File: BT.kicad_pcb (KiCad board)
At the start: 4 copper layers, 55 x 40 mm, 84 parts, among them J1 Conn_01x05_Pin, J2 Conn_01x03_Pin, J3 Conn_01x06_Pin, J5 Conn_02x03_Odd_Even, K1 AGQ200S12Z, Q1 BSS123, U1 PCM5100A, U2 ESP32-WROOM-32U, U3 TLV4888DR, U4 AP64060WU-7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

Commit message: integrated DAC in database
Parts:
- U1: footprint Package_SO:TSSOP-20_4.4x6.5mm_P0.65mm -> NRD_IC_DATA:PCM510xx
- moved C11 178.1 mm to (311.1, 121.3), turned to 0 degrees
- moved C7 176.0 mm to (311.1, 118.8), turned to 0 degrees
- moved C13 175.6 mm to (315.3, 119.0), turned to 0 degrees
- moved C12 174.1 mm to (311.1, 123.8), turned to 0 degrees
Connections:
- net Net-(U4-EN) renamed /+12V_FUSED

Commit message: wip
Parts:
- removed C28: 100nF, NRD_CAP:C_0603
- removed J5: Conn_02x03_Odd_Even, Connector_PinHeader_1.27mm:PinHeader_2x03_P1.27mm_Vertical_SMD
- removed L1, L2: 8.2uH, NRD_IND:74438367082
- removed U7: AP64060WU-7, NRD_IC_DCDC:AP6406x
- added C22: 2.2uF, NRD_CAP:C_0805, F.Cu at (182.1, 89.5)
- added C23: 4.7uF, NRD_CAP:C_1206, F.Cu at (196.0, 89.7)
- added C33: 2.2uF, NRD_CAP:C_0805, F.Cu at (182.1, 92.5)
- added C34: 2.2uF, NRD_CAP:C_0805, F.Cu at (182.1, 95.5)
- added C35: 100nF, NRD_CAP:C_0603, F.Cu at (181.9, 101.3)
- added C36: 2.2uF, NRD_CAP:C_0805, F.Cu at (182.1, 98.5)
- added FB2: 4k7@100MHz, Inductor_SMD:L_0805_2012Metric, F.Cu at (195.5, 92.7)
- added FB4: 4k7@100MHz, Inductor_SMD:L_0805_2012Metric, F.Cu at (195.5, 95.5)
- added J4: Boxed_Header_02x03_SMT, NRD_CON:Boxed_Header_02x03_SMT, F.Cu at (145.0, 102.2)
- added R32: 13K7, NRD_RES:R_0603, F.Cu at (181.9, 103.8)
- added RV1: 10K, Potentiometer_SMD:Potentiometer_Bourns_TC33X_Vertical, F.Cu at (152.8, 90.8)
- added U5: TLVM23615RDNR, NRD_IC_DCDC:TxxM336x5, F.Cu at (187.5, 103.1)
- C11, C7: footprint NRD_CAP:C_0603 -> NRD_CAP:C_0805
- C14, C15: value 220nF -> 2.2uF; footprint NRD_CAP:C_0603 -> NRD_CAP:C_0805
- C17: value 100nF -> 4.7uF; footprint NRD_CAP:C_0603 -> NRD_CAP:C_1206
- C18: value 2.2uF -> 100nF
- C19: value 10uF -> 4.7uF; footprint NRD_CAP:C_0805 -> NRD_CAP:C_1206
- C20: value 22uF -> 100nF; footprint NRD_CAP:C_0805 -> NRD_CAP:C_0603
- C21: value 22uF -> 4.7uF; footprint NRD_CAP:C_0805 -> NRD_CAP:C_1206
- C24, C25: value 10uF -> 22uF; footprint NRD_CAP:C_0805 -> NRD_CAP:C_1206
- C26: value 1uF -> 4.7uF; footprint NRD_CAP:C_0603 -> NRD_CAP:C_1206
- C29: value 2.2uF -> 22uF; footprint NRD_CAP:C_0603 -> NRD_CAP:C_1206
- C30: value 100nF -> 22uF; footprint NRD_CAP:C_0603 -> NRD_CAP:C_1206
- C31, C32: value 10uF -> 100nF; footprint NRD_CAP:C_0805 -> NRD_CAP:C_0603
- J3: value Conn_01x06_Pin -> S6B-PH-K-S; footprint Connector_JST:JST_PH_S6B-PH-K_1x06_P2.00mm_Horizontal -> NRD_CON:S6B-PH-K-S
- Q1: footprint Package_TO_SOT_SMD:SOT-23 -> NRD_MOSFET:BSS123
- R17, R19: value 0R -> 10K
- R18: value 2K -> 10K
- R2: value 10K -> 34K; footprint NRD_R_Var:3296P -> NRD_RES:R_0603
- R20: value 35K7 -> 2K
- R31: value 11K5 -> 21K
- R5: value 13K -> 14K3
- U2: footprint RF_Module:ESP32-WROOM-32U -> NRD_IC_MCU:WROOM_32U
- U4: value AP64060WU-7 -> TLVM23615RDNR; footprint NRD_IC_DCDC:AP6406x -> NRD_IC_DCDC:TxxM336x5
- U6: value TPS7A4701 -> RAA214220; footprint NRD_LDO:TPS7A47x -> NRD_LDO:RAA214220
- moved R2 37.7 mm to (186.4, 110.4)
- moved J3 5.55 mm to (171.6, 88.7)
- moved TP1 4.10 mm to (145.2, 92.0)
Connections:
- C17 pad 1: /BST_+6V -> +12V
- C17 pad 2: Net-(U4-SW) -> GND
- C18 pad 1: /+12V_FUSED -> +12V
- C19 pad 1: +5V -> +12V
- C20 pad 1: +3.3VA -> +12V
- C21 pad 1: +3.3VA -> Net-(U6-VOUT)
- C24 pad 1: +6V -> +3V3
- C25 pad 1: +6V -> +3V3
- C26 pad 1: Net-(U6-NR) -> Net-(U5-VCC)
- C27 pad 1: +5V -> Net-(U3E-V+)
- C30 pad 1: /BST_+3V3 -> +6V
- C30 pad 2: Net-(U7-SW) -> GND
- C32 pad 1: +3V3 -> Net-(C32-Pad1)
- F1 pad 1: /+12V_FUSED -> +12V
- F1 pad 2: +12V -> /KL30
- J3 pad 1: +12V -> /KL30
- R17 pad 1: Net-(U6-0.1V) -> +6V
- R17 pad 2: GND -> Net-(U5-FB)
- R18 pad 1: /FB_+6V -> Net-(U4-RT)
- R19 pad 1: Net-(U6-3.2V) -> Net-(U5-RT)
- R2 pad 1: Net-(C14-Pad2) -> +3V3
- R2 pad 2: GND -> Net-(U4-FB)
- R20 pad 1: +3V3 -> Net-(U5-FB)
- R20 pad 2: /FB_+3V3 -> GND
- R25 pad 1: Net-(R2-Pad3) -> Net-(R25-Pad1)
- R26 pad 2: Net-(R2-Pad3) -> Net-(R25-Pad1)
- R29 pad 2: Net-(R2-Pad3) -> Net-(R25-Pad1)
- R31 pad 1: /FB_+3V3 -> Net-(U6-VOUT)
- R31 pad 2: GND -> Net-(U6-ADJ)
- R5 pad 1: +6V -> Net-(U4-FB)
- R5 pad 2: /FB_+6V -> GND
- U3 pad 4: +5V -> Net-(U3E-V+)
- U4 pad 1: /BST_+6V -> unconnected-(U4-PGOOD-Pad1)
- U4 pad 2: GND -> +12V
- U4 pad 3: /FB_+6V -> +12V
- U4 pad 4: /+12V_FUSED -> +3V3
- U4 pad 5: /+12V_FUSED -> unconnected-(U4-SW-Pad5)_4
- U4 pad 6: Net-(U4-SW) -> unconnected-(U4-SW_2-Pad6)
- U6 pad 1: +3.3VA -> +3V3
- U6 pad 2: unconnected-(U6-NC-Pad2) -> GND
- U6 pad 3: +3.3VA -> +3V3
- U6 pad 4: unconnected-(U6-6.4V-Pad4) -> Net-(U6-ADJ)
- U6 pad 5: unconnected-(U6-6.4V-Pad5) -> Net-(U6-VOUT)

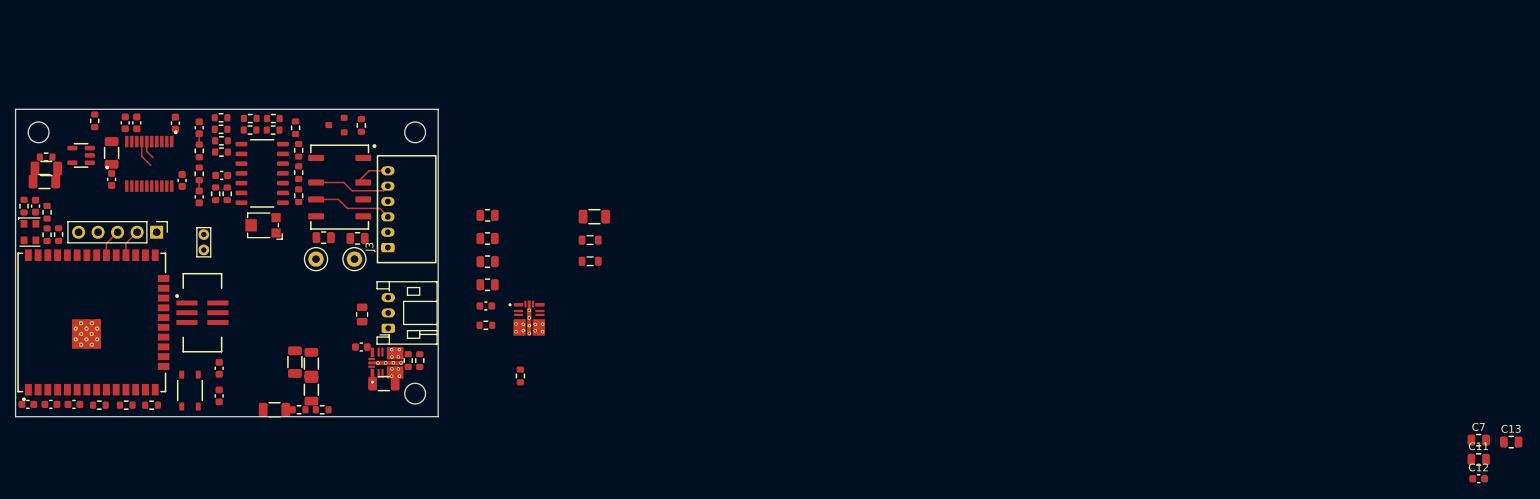
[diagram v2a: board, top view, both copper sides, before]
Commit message: rough placement PSU
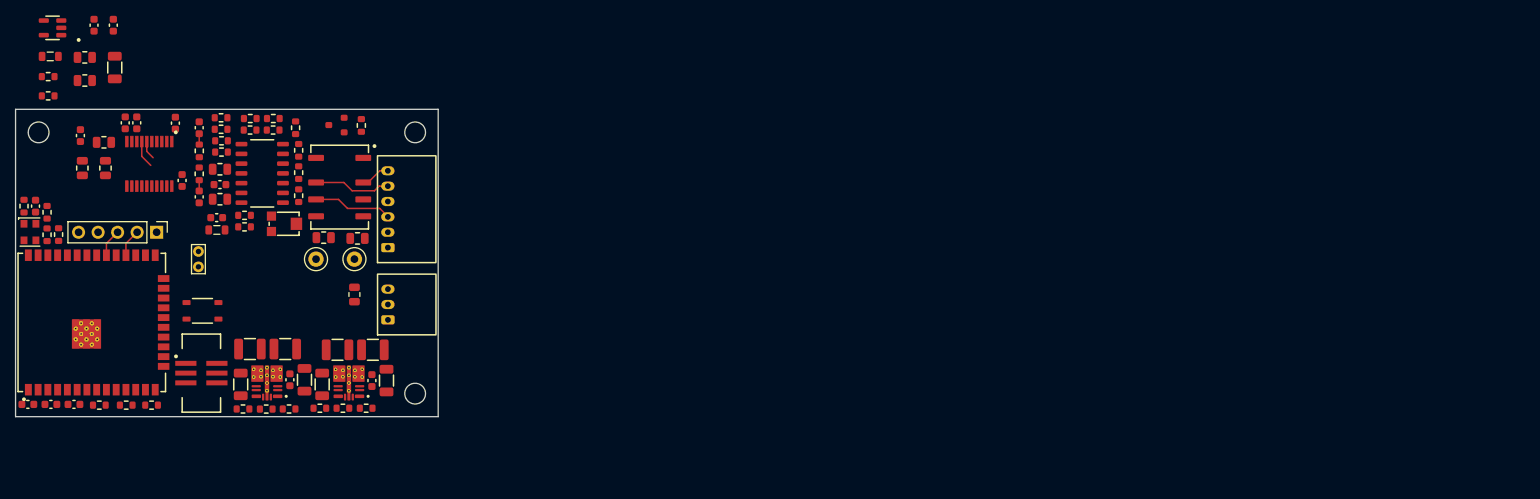
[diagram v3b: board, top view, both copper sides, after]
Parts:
- removed RV1: 10K, Potentiometer_SMD:Potentiometer_Bourns_TC33X_Vertical
- added R33: 10K, NRD_R_Var:TC33X-2, F.Cu at (155.8, 90.6)
- C24, C25, C29, C30: footprint NRD_CAP:C_1206 -> NRD_CAP:C_1210
- J2: value Conn_01x03_Pin -> S3B-PH-K-S; footprint Connector_JST:JST_PH_S3B-PH-K_1x03_P2.00mm_Horizontal -> NRD_CON:S3B-PH-K-S
- S1: value ~ -> 434123025826
- moved C12 187.4 mm to (129.1, 79.1), turned to 90 degrees
- moved C13 186.4 mm to (132.4, 83.4), turned to 90 degrees
- moved C11 185.6 mm to (129.4, 83.4), turned to 90 degrees
- moved C7 183.1 mm to (132.2, 80.0)
- moved FB2 74.2 mm to (125.2, 68.8)
- moved R32 64.3 mm to (124.9, 74.0)
- moved C22 56.3 mm to (129.7, 69.0)
- moved C33 56.3 mm to (129.7, 72.0)
- moved R31 56.1 mm to (124.9, 71.5)
- moved C31 50.9 mm to (130.9, 64.8)
- moved FB4 48.7 mm to (146.9, 91.4), turned to 180 degrees
- moved C32 46.7 mm to (133.4, 64.8)
- moved R19 45.2 mm to (156.3, 114.7), turned to 0 degrees
- moved C20 42.8 mm to (167.1, 111.0), turned to 90 degrees
- moved C19 42.6 mm to (158.3, 110.9), turned to 90 degrees
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
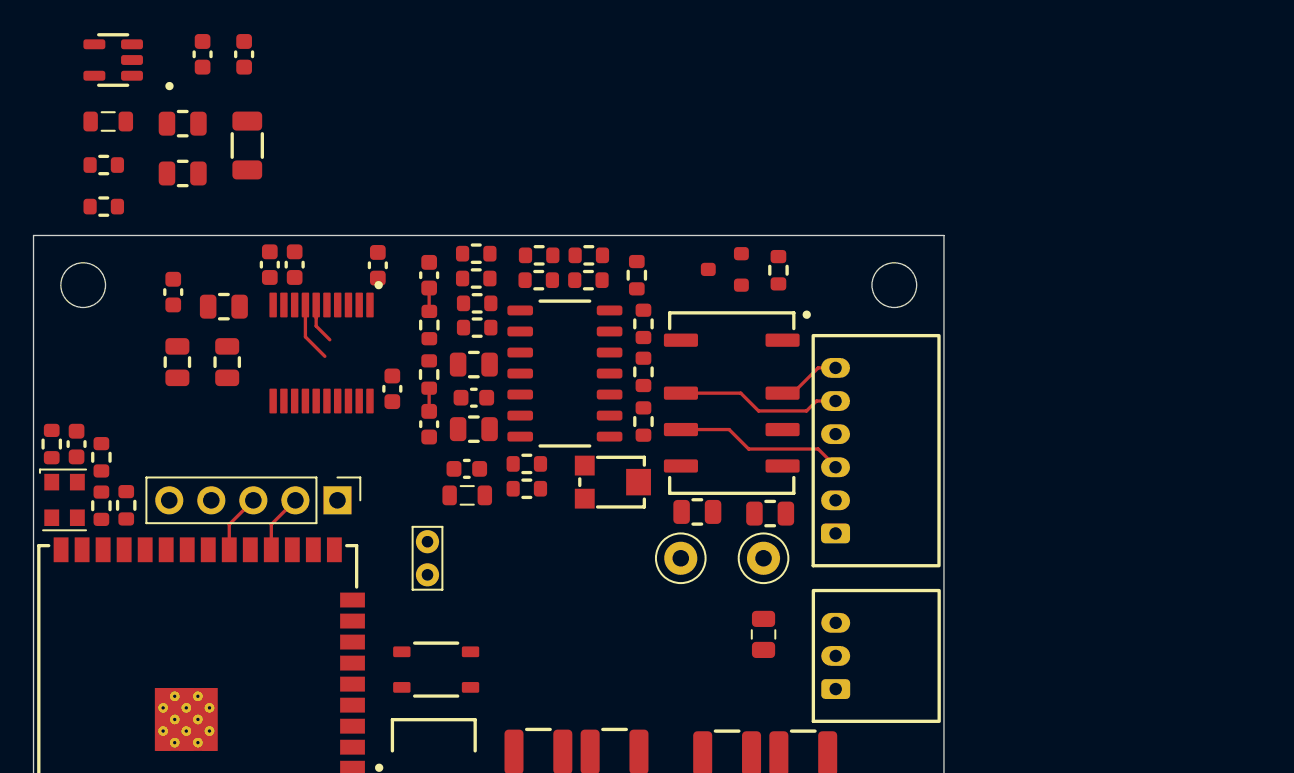
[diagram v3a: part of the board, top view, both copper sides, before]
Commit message: replaced all components by library parts
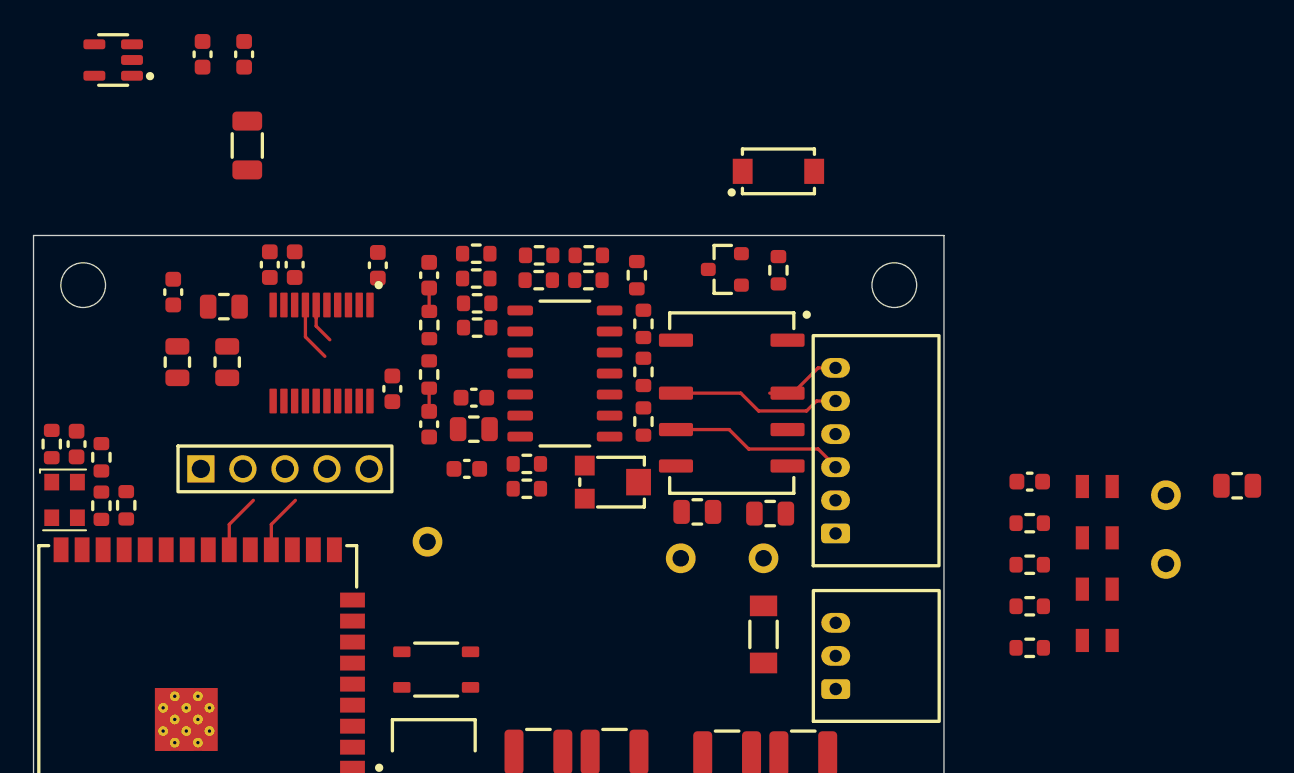
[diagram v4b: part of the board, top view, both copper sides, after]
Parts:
- removed C34: 2.2uF, NRD_CAP:C_0805
- removed FB2, FB4: 4k7@100MHz, Inductor_SMD:L_0805_2012Metric
- added D1: VSSAF5N50-M3/6B, NRD_Diodes:VSSAF5N50, F.Cu at (165.7, 71.8)
- added L1: 10uH, NRD_IND:74479777310, F.Cu at (184.9, 90.9)
- added L2: 10uH, NRD_IND:74479777310, F.Cu at (184.9, 94.0)
- added L3: 10uH, NRD_IND:74479777310, F.Cu at (184.9, 97.1)
- added L4: 10uH, NRD_IND:74479777310, F.Cu at (184.9, 100.2)
- added R34: 10K, NRD_RES:R_0603, F.Cu at (180.9, 98.1)
- added R35: 1K, NRD_RES:R_0603, F.Cu at (180.9, 100.6)
- added TP4: 5001, NRD_MISC:500x, F.Cu at (189.1, 91.4)
- added TP5: 5001, NRD_MISC:500x, F.Cu at (189.1, 95.5)
- C22: value 2.2uF -> 100nF; footprint NRD_CAP:C_0805 -> NRD_CAP:C_0603
- F1: value Fuse -> SF-1206S050-2; footprint Fuse:Fuse_0805_2012Metric -> NRD_Fuse:SF-1206S
- J1: value Conn_01x05_Pin -> 61300511121; footprint Connector_PinHeader_2.54mm:PinHeader_1x05_P2.54mm_Vertical -> NRD_PinHeader:61300511121
- J2: value S3B-PH-K-S -> Conn_01x03_Pin
- K1: value AGQ200S12Z -> AGQ200A12Z; footprint NRD_Relays:AGQ200Sxxx -> NRD_Relays:AGQ200Axxx
- M1: renamed from H1; value MountingHole -> (none); footprint MountingHole:MountingHole_2.7mm_M2.5_ISO7380 -> NRD_MECH:Mounting_Hole_2.7mm_Unplated
- M2: renamed from H2; value MountingHole -> (none); footprint MountingHole:MountingHole_2.7mm_M2.5_ISO7380 -> NRD_MECH:Mounting_Hole_2.7mm_Unplated
- M3: renamed from H3; value MountingHole -> (none); footprint MountingHole:MountingHole_2.7mm_M2.5_ISO7380 -> NRD_MECH:Mounting_Hole_2.7mm_Unplated
- S1: value 434123025826 -> Untitled
- TP1: value TestPoint -> 5001; footprint TestPoint:TestPoint_Bridge_Pitch2.0mm_Drill0.7mm -> NRD_MISC:500x
- TP2, TP3: value TestPoint -> 5001; footprint TestPoint:TestPoint_Loop_D2.50mm_Drill1.0mm -> NRD_MISC:500x
- moved C33 66.4 mm to (193.4, 90.8)
- moved R31 60.0 mm to (180.9, 93.1)
- moved R32 60.0 mm to (180.9, 95.6)
- moved C22 55.5 mm to (180.9, 90.6)
- moved J1 3.70 mm to (135.9, 89.8), turned to 0 degrees
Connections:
- net /DAC_MUTE renamed /DAC_MUTEn
- net Net-(U6-ADJ) renamed /+3V3A_FB
- C21 pad 1: Net-(U6-VOUT) -> /+3V3A_OUT
- C22 pad 1: Net-(U6-VOUT) -> /Button
- J2 pad 2: /Button -> Net-(J2-Pin_2)
- R31 pad 1: Net-(U6-VOUT) -> /+3V3A_OUT
- R7 pad 2: GND -> +3V3
- U6 pad 5: Net-(U6-VOUT) -> /+3V3A_OUT
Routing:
- net /DIN: track 3.59 -> 0.00 mm
- net /BCK: track 0.00 -> 3.59 mm

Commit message: started layout
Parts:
- removed TP4, TP5: 5001, NRD_MISC:500x
- J2: value Conn_01x03_Pin -> S3B-PH-K-S
- M1, M2, M3: value (none) -> Mounting_Hole_2.7mm_Unplated
- S1: value Untitled -> 434123025826
- moved C33 62.1 mm to (132.7, 77.7), turned to 90 degrees
- moved L3 59.0 mm to (128.6, 79.5), turned to 90 degrees
- moved L4 58.1 mm to (130.7, 79.5), turned to -90 degrees
- moved R31 52.6 mm to (129.1, 84.1)
- moved R34 50.5 mm to (139.5, 69.3)
- moved R32 50.2 mm to (132.0, 84.1)
- moved C22 49.1 mm to (137.3, 113.2)
- moved R35 48.3 mm to (134.3, 113.2)
- moved L2 38.1 mm to (147.3, 87.9)
- moved L1 37.7 mm to (147.3, 91.4), turned to 180 degrees
- moved R6 32.8 mm to (166.0, 103.1), turned to 180 degrees
- moved R17 20.9 mm to (169.4, 106.2), turned to 180 degrees
- moved C31 20.2 mm to (122.8, 83.2)
- moved C17 19.1 mm to (149.9, 109.3), turned to -90 degrees
- moved C11 19.0 mm to (144.0, 71.1)
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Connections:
- net Net-(J2-Pin_1) renamed /LED_CON
- net Net-(J2-Pin_2) renamed /BUTTON_CON
- net Net-(U4-FB) renamed /FB_+3V3
- J1 pad 2: /LRCK -> /BCK
- J1 pad 4: /BCK -> /LRCK
- U2 pad 28: /BCK -> /LRCK
- U2 pad 29: unconnected-(U2-IO5-Pad29) -> /DIN
- U2 pad 30: /LRCK -> unconnected-(U2-IO18-Pad30)
- U2 pad 31: /DIN -> /BCK
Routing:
- net Net-(C14-Pad2): track 0.00 -> 42.2 mm, vias 0 -> 2
- net +6V: track 0.00 -> 40.1 mm, vias 0 -> 3
- net GND: track 0.00 -> 38.0 mm, vias 0 -> 32
- net /ESP_EN: track 0.00 -> 36.2 mm, vias 0 -> 3
- net +12V: track 0.00 -> 34.5 mm, vias 0 -> 2
- net /ESP_RXD0: track 0.00 -> 30.2 mm
- net /ESP_TXD0: track 0.00 -> 26.7 mm
- net +3V3: track 0.00 -> 26.5 mm, vias 0 -> 8
- net /ESP_IO0: track 0.00 -> 21.5 mm
- net Net-(C8-Pad1): track 1.40 -> 21.0 mm, vias 0 -> 2
- net Net-(R25-Pad1): track 0.00 -> 18.6 mm, vias 0 -> 2
- net Net-(U3B-+): track 0.00 -> 15.9 mm, vias 0 -> 2
- net /KL30: track 0.00 -> 12.0 mm
- net /SCK: track 0.00 -> 11.8 mm, vias 0 -> 1
- net Net-(U3C-+): track 0.00 -> 10.1 mm
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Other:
- board text added: "+3V3"
- board text added: "BCK"
- board text added: "DIN"
- board text added: "GND"
- board text added: "LRCK"

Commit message: almost finished layout. Something is still off in the design rules
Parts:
- J2: value S3B-PH-K-S -> Conn_01x03_Pin
- M1, M2, M3: value Mounting_Hole_2.7mm_Unplated -> (none)
- S1: value 434123025826 -> Untitled
- moved R34 22.8 mm to (128.0, 88.9), turned to -90 degrees
- moved C12 21.9 mm to (138.8, 88.2), turned to 180 degrees
- moved C13 17.8 mm to (142.0, 88.2), turned to 0 degrees
- moved C7 12.5 mm to (140.1, 78.3), turned to 180 degrees
- moved C11 9.24 mm to (137.4, 77.6)
- moved TP1 8.36 mm to (152.8, 95.2)
- moved J1 2.47 mm to (135.9, 91.0)
- moved R15 1.20 mm to (125.0, 87.0)
- moved C8 0.85 mm to (144.9, 89.0)
- moved R6 0.83 mm to (166.2, 102.3), turned to 90 degrees
- moved C5 0.73 mm to (122.3, 113.9)
- moved C6 0.73 mm to (125.3, 113.9)
- moved C10 0.73 mm to (128.3, 113.9), turned to 180 degrees
- moved R3 0.73 mm to (131.3, 113.9)
- moved R35 0.73 mm to (134.3, 113.9)
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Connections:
- C3 pad 1: +3.3VA -> +3V3A
- C4 pad 1: +3.3VA -> +3V3A
- U1 pad 8: +3.3VA -> +3V3A
- U2 pad 10: /DAC_FMT -> unconnected-(U2-IO25-Pad10)
- U2 pad 30: unconnected-(U2-IO18-Pad30) -> /DAC_FLT
- U2 pad 33: /DAC_FLT -> /DAC_FMT
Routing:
- net /SW_TO_BT_AUDIO: track 0.00 -> 77.0 mm, vias 0 -> 2
- net /BUTTON_CON: track 1.01 -> 42.4 mm
- net /LED: track 0.00 -> 37.6 mm, vias 0 -> 2
- net GND: track 38.0 -> 73.0 mm, vias 32 -> 58
- net /DAC_MCLK_EN: track 0.00 -> 28.4 mm, vias 0 -> 2
- net /DAC_MUTEn: track 0.00 -> 26.3 mm, vias 0 -> 3
- net /DAC_DMP: track 0.00 -> 18.7 mm
- net /DAC_FMT: track 0.00 -> 16.5 mm
- net Net-(R24-Pad1): track 2.00 -> 17.6 mm, vias 0 -> 2
- net /DAC_FLT: track 0.00 -> 13.5 mm, vias 0 -> 2
- net /MCLK: track 0.00 -> 12.1 mm, vias 0 -> 2
- net +3V3: track 26.5 -> 33.7 mm, vias 8 -> 12
- net /SCK: track 11.8 -> 17.6 mm, vias 1 -> 2
- net /+3V3A_FB: track 0.00 -> 5.28 mm
- net Net-(U1-LDOO): track 0.00 -> 3.78 mm
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- added copper zone on F.Cu, net +12V
- added copper zone on F.Cu, net +3V3
- added copper zone on In2.Cu, net +3V3
- added copper zone on F.Cu, net +3V3A
- added copper zone on F.Cu, net /+3V3A_OUT
- added copper zone on B.Cu, net GND
- added copper zone on F.Cu, net GND
- added copper zone on In1.Cu, net GND
- added copper zone on F.Cu, net Net-(C32-Pad1)
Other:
- board text removed: "+3V3"
- board text removed: "BCK"
- board text removed: "DIN"
- board text removed: "GND"
- board text removed: "LRCK"
